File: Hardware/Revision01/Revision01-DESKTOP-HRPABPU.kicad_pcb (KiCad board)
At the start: 4 copper layers, 100 x 99.6 mm, 104 parts, among them J1 Conn_01x05, J10 StrainConn, J11 StrainConn, J12 StrainConn, J14 Conn_01x05, J15 Conn_01x09, J2 Conn_01x02, J3 Conn_01x02, J4 Battery connector, J5 StrainConn, J6 StrainConn, J7 StrainConn, J8 StrainConn, J9 StrainConn, Q1 PMOS, Q2 NMOS, Q3 PMOS, SW1 ON/OFF_SW_SPST_LED, U1 NUCLEO-L476RG, U3 MPU-6500, U6 LMR51603XFDBVR

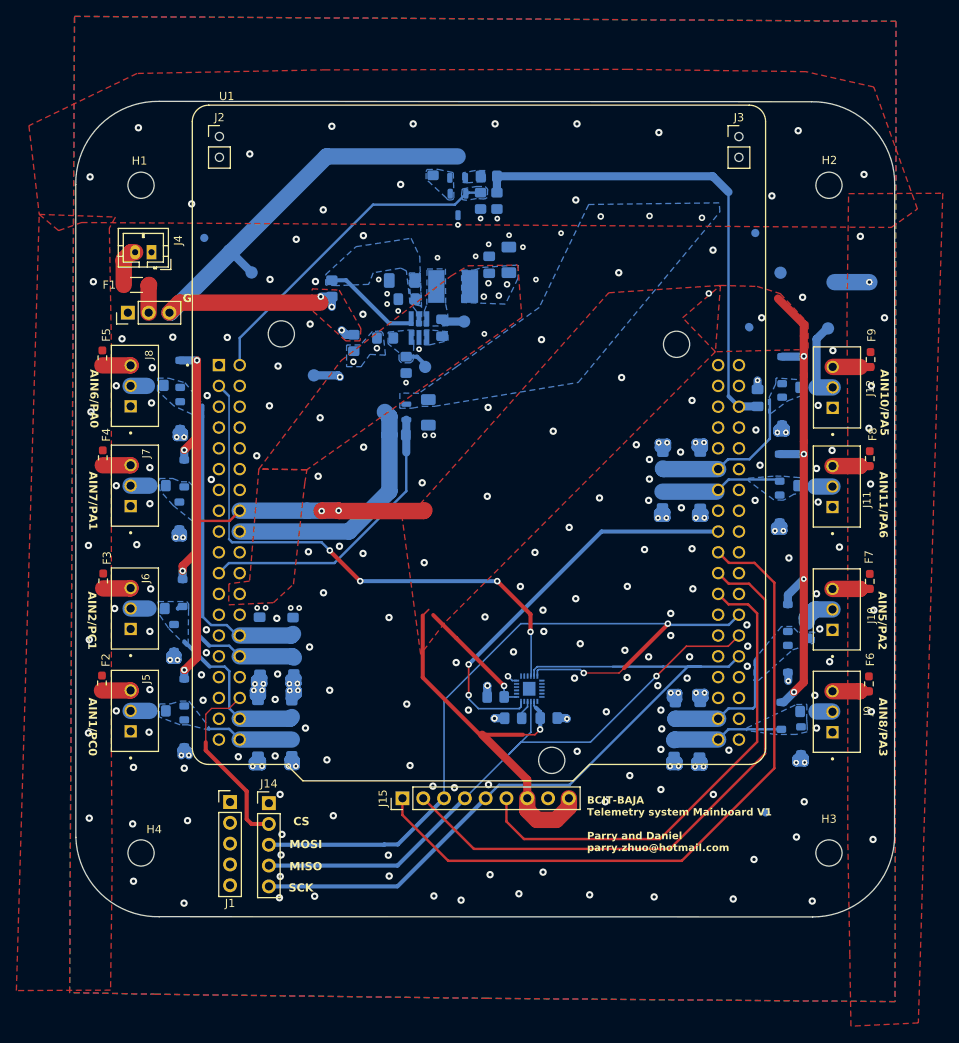
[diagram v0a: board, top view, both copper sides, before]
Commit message: review 2 implemented
- Made mounting holes symmetrical
- Buck enable 0 ohm resistor error fixed
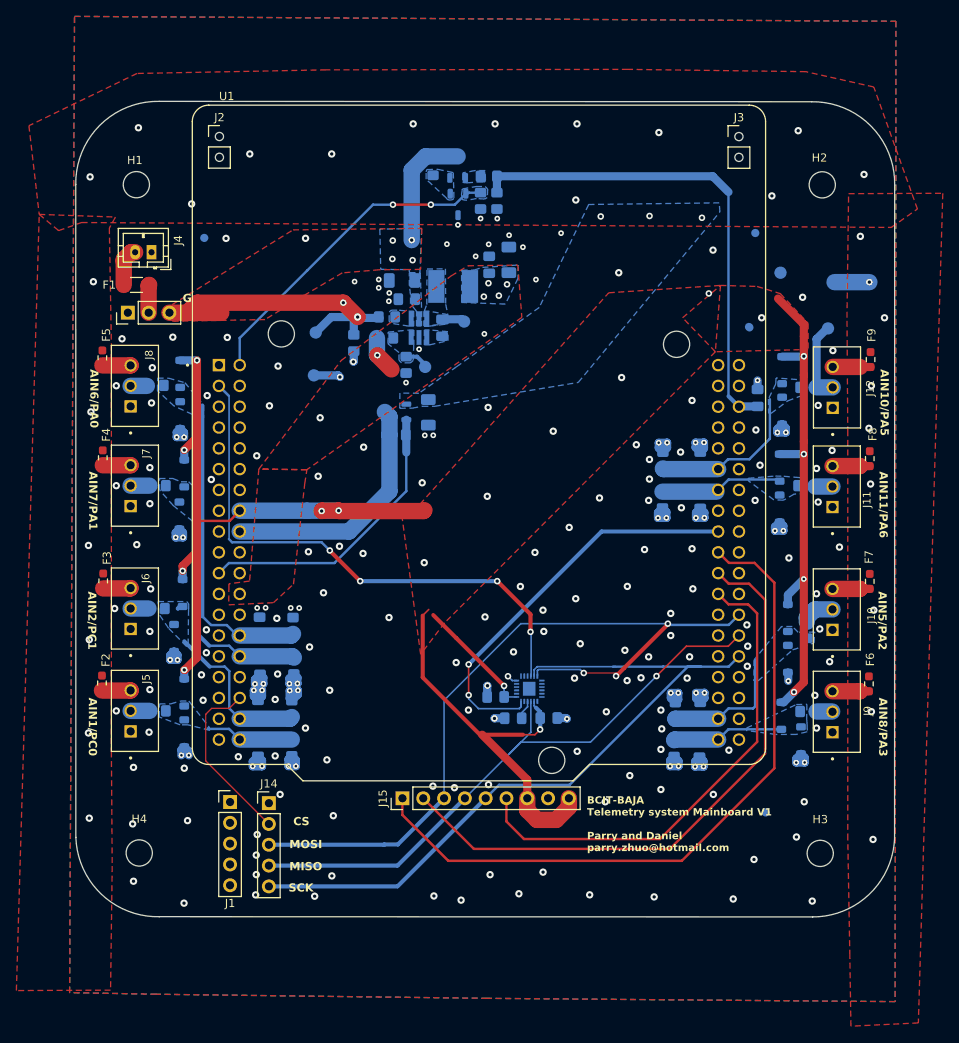
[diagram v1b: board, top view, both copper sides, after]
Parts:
- moved TP4 10.7 mm to (140.3, 71.0)
- moved H2 8.82 mm to (202.2, 53.0)
- moved R33 7.58 mm to (149.0, 69.1), turned to 0 degrees
- moved H3 1.07 mm to (201.9, 134.6)
- moved H1 0.57 mm to (118.4, 52.9)
- moved H4 0.34 mm to (118.8, 134.5)
- turned R36 to -90 degrees
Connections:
- C20 pad 1: Net-(U6-EN) -> +V_batt
- C21 pad 1: Net-(U6-EN) -> +V_batt
- R33 pad 2: Net-(U6-EN) -> /BuckEnable
- R36 pad 1: +Vin_7V -> +V_batt
- R36 pad 2: +V_batt -> +Vin_7V
- U6 pad 4: Net-(U6-EN) -> /BuckEnable
- U6 pad 5: Net-(U6-EN) -> +V_batt
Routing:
- net Net-(U6-EN): track 11.9 -> 0.00 mm
- net +V_batt: track 70.0 -> 58.6 mm, vias 3 -> 6
- net +Vin_7V: track 3.27 -> 9.15 mm
- net /PB15_SPI2_MOSI: track 95.5 -> 96.9 mm, vias 2 -> 3
- net /~{CANBUS_CS_GPIO}: track 22.9 -> 21.6 mm
- net GND: vias 252 -> 243
- net /BatteryV_Div_Enable_GPIO: vias 0 -> 2
- added copper zone on B.Cu, net +V_batt
- added copper zone on B.Cu, net /BuckEnable
- removed copper zone on B.Cu, net Net-(U6-EN)
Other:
- board text added: "BuckEN->Disable"
- board text removed: "Buck-En"
